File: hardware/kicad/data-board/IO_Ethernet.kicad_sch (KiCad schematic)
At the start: 44 parts, among them J3 BMS I2C, SW1 Wake, U3 MagJack-A70-112-331N126, U5 74LVC1G07SE-7, U9 74LVC1G07SE-7

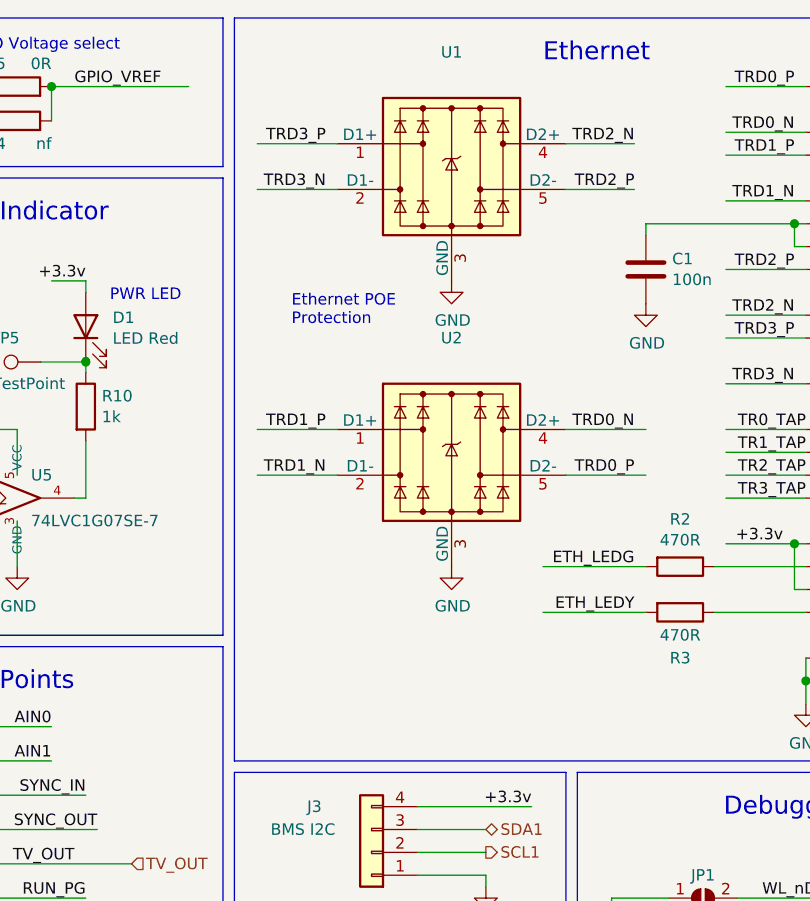
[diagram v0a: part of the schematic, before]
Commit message: breaks out PoE ttap
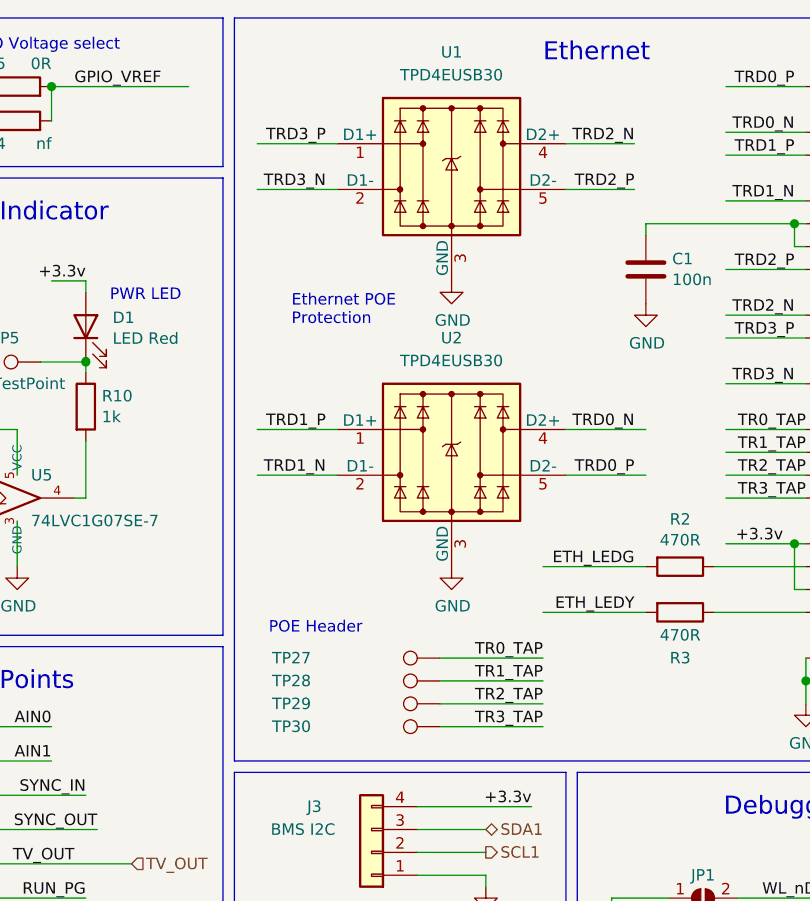
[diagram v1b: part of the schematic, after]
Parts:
- added TP27, TP28, TP29, TP30: (no value), symbol Connector:TestPoint
- U1, U2: value (none) -> TPD4EUSB30; footprint (none) -> Package_SON:USON-10_2.5x1.0mm_P0.5mm
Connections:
- net TR0_TAP: now also TP27.1
- net TR1_TAP: now also TP28.1
- net TR2_TAP: now also TP29.1
- net TR3_TAP: now also TP30.1
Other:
- note added: "POE Header"
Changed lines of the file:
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@@
+    (stroke (width 0) (type solid) (color 0 0 0 0))
+  )
+  (wire (pts (xy 217.17 92.71) (xy 205.74 92.71))
     (stroke (width 0) (type solid) (color 0 0 0 0))
   )
@@
     (stroke (width 0) (type solid) (color 0 0 0 0))
   )
+  (wire (pts (xy 217.17 90.17) (xy 205.74 90.17))
+    (stroke (width 0) (type solid) (color 0 0 0 0))
+  )
   (wire (pts (xy 228.6 38.1) (xy 228.6 36.83))
     (stroke (width 0) (type solid) (color 0 0 0 0))
@@
     (stroke (width 0) (type solid) (color 0 0 0 0))
   )
+  (wire (pts (xy 205.74 85.09) (xy 217.17 85.09))
+    (stroke (width 0) (type solid) (color 0 0 0 0))
+  )
   (wire (pts (xy 154.94 100.33) (xy 166.37 100.33))
     (stroke (width 0) (type default) (color 0 0 0 0))
@@
   )
   (wire (pts (xy 100.076 107.95) (xy 101.346 107.95))
+    (stroke (width 0) (type solid) (color 0 0 0 0))
+  )
+  (wire (pts (xy 205.74 87.63) (xy 217.17 87.63))
     (stroke (width 0) (type solid) (color 0 0 0 0))
   )
@@
   (text "Debugging Jumper" (at 262.89 102.87 180)
     (effects (font (size 2 2)) (justify right bottom))
+  )
+  (text "POE Header" (at 186.69 82.55 0)
+    (effects (font (size 1.27 1.27)) (justify left bottom))
   )
   (text "UART Console" (at 212.09 123.19 180)
@@
     (effects (font (size 1.27 1.27)) (justify right bottom))
   )
+  (label "TR1_TAP" (at 217.17 87.63 180)
+    (effects (font (size 1.27 1.27)) (justify right bottom))
+  )
   (label "nPWR_LED" (at 114.046 138.43 180)
     (effects (font (size 1.27 1.27)) (justify right bottom))
@@
     (effects (font (size 1.27 1.27)) (justify right bottom))
   )
+  (label "TR2_TAP" (at 217.17 90.17 180)
+    (effects (font (size 1.27 1.27)) (justify right bottom))
+  )
   (label "SYNC_IN" (at 166.37 100.33 180)
     (effects (font (size 1.27 1.27)) (justify right bottom))
@@
   )
   (label "TXD0" (at 213.36 133.35 180)
+    (effects (font (size 1.27 1.27)) (justify right bottom))
+  )
+  (label "TR3_TAP" (at 217.17 92.71 180)
     (effects (font (size 1.27 1.27)) (justify right bottom))
   )
@@
   (label "TRD3_P" (at 102.87 21.59 0)
     (effects (font (size 1.27 1.27)) (justify left bottom))
+  )
+  (label "TR0_TAP" (at 217.17 85.09 180)
+    (effects (font (size 1.27 1.27)) (justify right bottom))
   )
   (label "TRD1_N" (at 30.226 24.13 180)
@@
     (pin "1")
   )
+  (symbol (lib_id "Connector:TestPoint") (at 205.74 85.09 90) (unit 1)
+    (in_bom yes) (on_board yes)
+    (property "Reference" "TP27" (id 0) (at 189.23 85.09 90))
+    (property "Value" "" (id 1) (at 196.85 85.09 90))
+    (property "Footprint" "" (id 2) (at 205.74 80.01 0)
+      (effects (font (size 1.27 1.27)) hide)
+    )
+    (property "Datasheet" "~" (id 3) (at 205.74 80.01 0)
+      (effects (font (size 1.27 1.27)) hide)
+    )
+    (pin "1")
+  )
   (symbol (lib_id "Connector:TestPoint") (at 205.74 137.16 90) (unit 1)
     (in_bom yes) (on_board yes)
@@
     (in_bom yes) (on_board yes) (fields_autoplaced)
     (property "Reference" "U1" (id 0) (at 207.01 17.78 0))
-    (property "Value" "" (id 1) (at 207.01 20.32 0))
-    (property "Footprint" "" (id 2) (at 182.88 40.64 0)
+    (property "Value" "TPD4EUSB30" (id 1) (at 207.01 20.32 0))
+    (property "Footprint" "Package_SON:USON-10_2.5x1.0mm_P0.5mm" (id 2) (at 182.88 40.64 0)
       (effects (font (size 1.27 1.27)) hide)
     )
@@
     (pin "1")
   )
+  (symbol (lib_id "Connector:TestPoint") (at 205.74 87.63 90) (unit 1)
+    (in_bom yes) (on_board yes)
+    (property "Reference" "TP28" (id 0) (at 189.23 87.63 90))
+    (property "Value" "" (id 1) (at 196.85 87.63 90))
+    (property "Footprint" "" (id 2) (at 205.74 82.55 0)
+      (effects (font (size 1.27 1.27)) hide)
+    )
+    (property "Datasheet" "~" (id 3) (at 205.74 82.55 0)
+      (effects (font (size 1.27 1.27)) hide)
+    )
+    (pin "1")
+  )
+  (symbol (lib_id "Connector:TestPoint") (at 205.74 92.71 90) (unit 1)
+    (in_bom yes) (on_board yes)
+    (property "Reference" "TP30" (id 0) (at 189.23 92.71 90))
+    (property "Value" "" (id 1) (at 196.85 92.71 90))
+    (property "Footprint" "" (id 2) (at 205.74 87.63 0)
+      (effects (font (size 1.27 1.27)) hide)
+    )
+    (property "Datasheet" "~" (id 3) (at 205.74 87.63 0)
+      (effects (font (size 1.27 1.27)) hide)
+    )
+    (pin "1")
+  )
   (symbol (lib_id "Jumper:SolderJumper_2_Open") (at 262.89 111.76 0) (unit 1)
     (in_bom yes) (on_board yes)
@@
     (pin "2")
   )
+  (symbol (lib_id "Connector:TestPoint") (at 205.74 90.17 90) (unit 1)
+    (in_bom yes) (on_board yes)
+    (property "Reference" "TP29" (id 0) (at 189.23 90.17 90))
+    (property "Value" "" (id 1) (at 196.85 90.17 90))
+    (property "Footprint" "" (id 2) (at 205.74 85.09 0)
+      (effects (font (size 1.27 1.27)) hide)
+    )
+    (property "Datasheet" "~" (id 3) (at 205.74 85.09 0)
+      (effects (font (size 1.27 1.27)) hide)
+    )
+    (pin "1")
+  )
   (symbol (lib_id "Connector:TestPoint") (at 205.74 140.97 90) (unit 1)
     (in_bom yes) (on_board yes)
@@
     (in_bom yes) (on_board yes) (fields_autoplaced)
     (property "Reference" "U2" (id 0) (at 207.01 49.53 0))
-    (property "Value" "" (id 1) (at 207.01 52.07 0))
-    (property "Footprint" "" (id 2) (at 182.88 72.39 0)
-      (effects (font (size 1.27 1.27)) hide)
-    )
+    (property "Value" "TPD4EUSB30" (id 1) (at 207.01 52.07 0))
+    (property "Footprint" "Package_SON:USON-10_2.5x1.0mm_P0.5mm" (id 2) (at 182.88 72.39 0)
+      (effects (font (size 1.27 1.27)) hide)
+    )

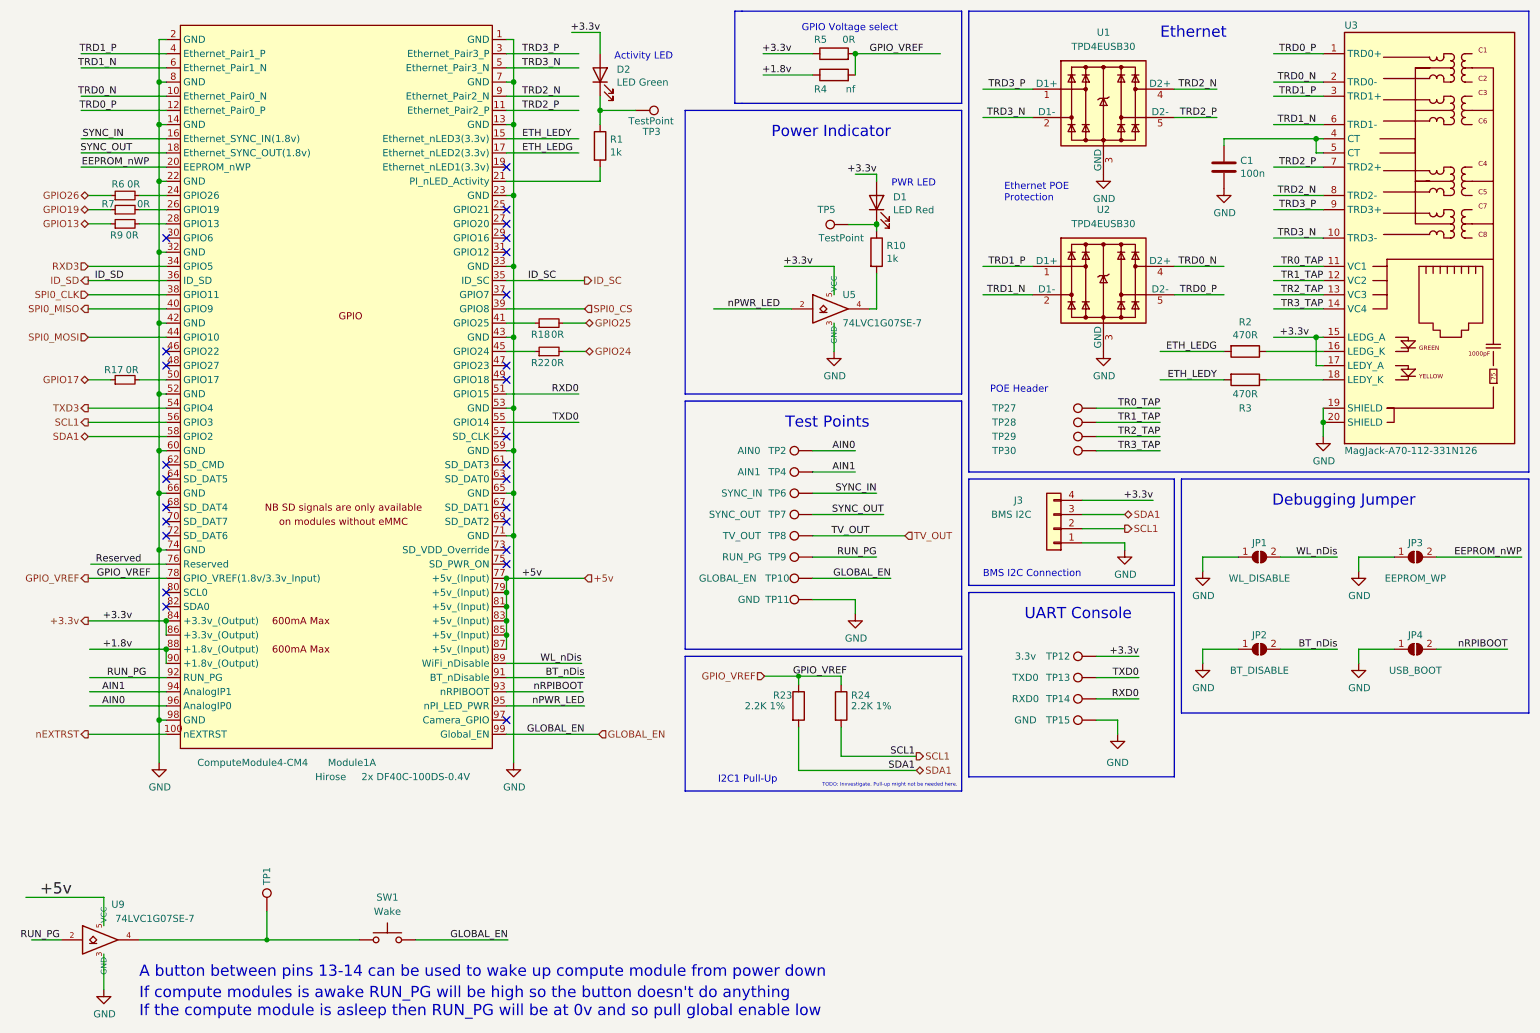
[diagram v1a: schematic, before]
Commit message: change poe tap location and change debug solder jumper to jst
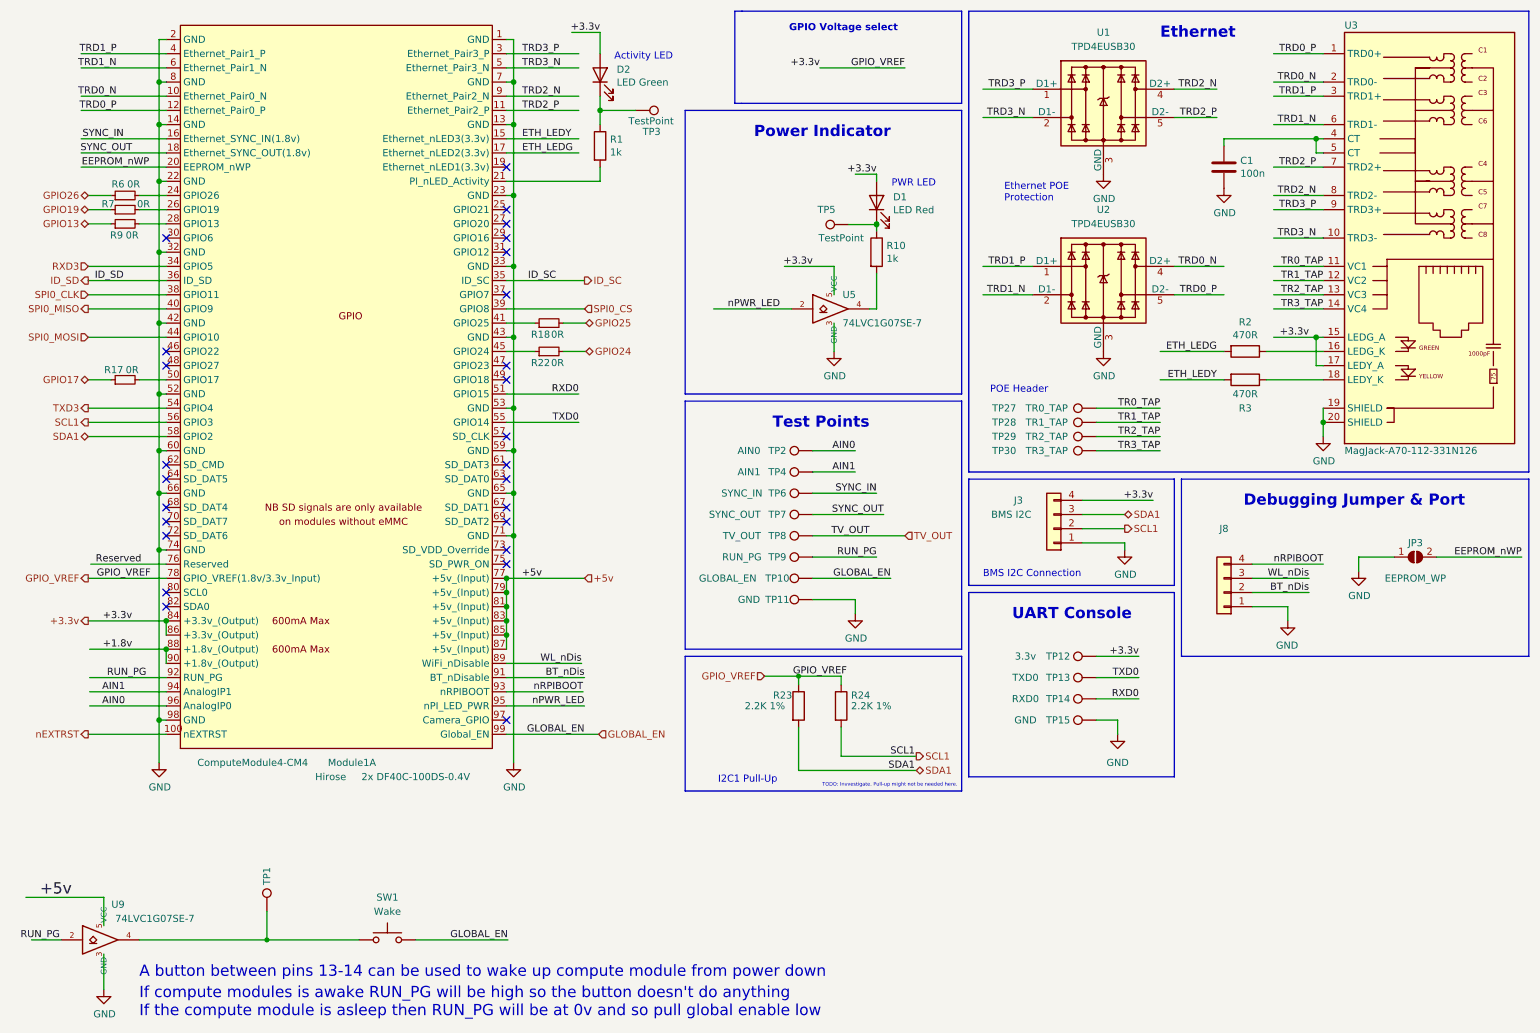
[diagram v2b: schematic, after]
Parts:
- removed JP1: WL_DISABLE, Jumper:SolderJumper-2_P1.3mm_Open_RoundedPad1.0x1.5mm, symbol Jumper:SolderJumper_2_Open
- removed JP2: BT_DISABLE, Jumper:SolderJumper-2_P1.3mm_Open_RoundedPad1.0x1.5mm, symbol Jumper:SolderJumper_2_Open
- removed JP4: USB_BOOT, Jumper:SolderJumper-2_P1.3mm_Open_RoundedPad1.0x1.5mm, symbol Jumper:SolderJumper_2_Open
- removed R4: nf, Resistor_SMD:R_0805_2012Metric_Pad1.15x1.40mm_HandSolder, symbol Device:R
- removed R5: 0R, Resistor_SMD:R_0805_2012Metric_Pad1.15x1.40mm_HandSolder, symbol Device:R
- added J8: (no value), symbol Connector_Generic:Conn_01x04
- TP27: value (none) -> TR0_TAP; footprint (none) -> TestPoint:TestPoint_Pad_D2.0mm
- TP28: value (none) -> TR1_TAP; footprint (none) -> TestPoint:TestPoint_Pad_D2.0mm
- TP29: value (none) -> TR2_TAP; footprint (none) -> TestPoint:TestPoint_Pad_D2.0mm
- TP30: value (none) -> TR3_TAP; footprint (none) -> TestPoint:TestPoint_Pad_D2.0mm
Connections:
- net GPIO_VREF is gone; now on net +3.3v: Module1.78 (GPIO_VREF(1.8v/3.3v_Input)), R23.1, R24.1
- net BT_nDis: now also J8.2 (Pin_2)
- net GND: now also J8.1 (Pin_1)
- net WL_nDis: now also J8.3 (Pin_3)
- net nRPIBOOT: now also J8.4 (Pin_4)
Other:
- note added: "Debugging Jumper & Port"
- note removed: "Debugging Jumper"

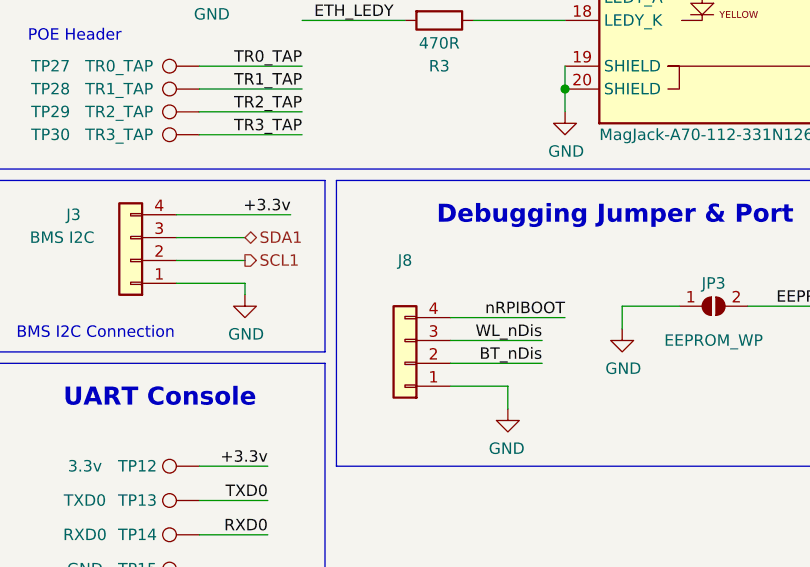
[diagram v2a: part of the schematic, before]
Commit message: fix incorrect fill rules
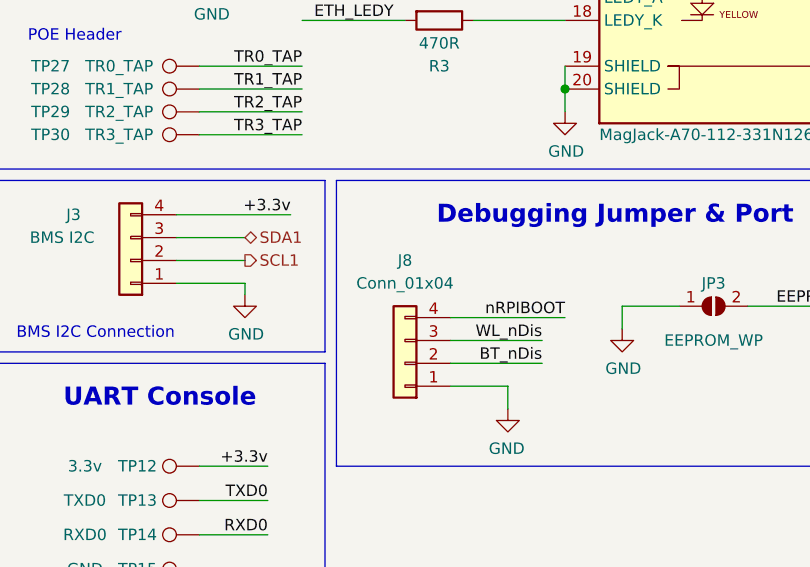
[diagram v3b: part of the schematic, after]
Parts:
- J8: value (none) -> Conn_01x04; footprint (none) -> Connector_Molex:Molex_Pico-Lock_504050-0591_1x05-1MP_P1.50mm_Horizontal
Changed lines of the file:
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@@
     (in_bom yes) (on_board yes) (fields_autoplaced)
     (property "Reference" "J8" (id 0) (at 228.6 106.68 0))
-    (property "Value" "" (id 1) (at 228.6 109.22 0))
-    (property "Footprint" "" (id 2) (at 228.6 118.11 0)
+    (property "Value" "Conn_01x04" (id 1) (at 228.6 109.22 0))
+    (property "Footprint" "Connector_Molex:Molex_Pico-Lock_504050-0591_1x05-1MP_P1.50mm_Horizontal" (id 2) (at 228.6 118.11 0)
       (effects (font (size 1.27 1.27)) hide)
     )
